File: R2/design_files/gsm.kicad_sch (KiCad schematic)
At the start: 23 parts, among them J4 Conn_Coaxial, J5 SIM_Card, M1 BG96, U3 PUMH10,115, U4 NXB0108PW, U5 AP22800HB-7, U6 DF6A6.8FUT

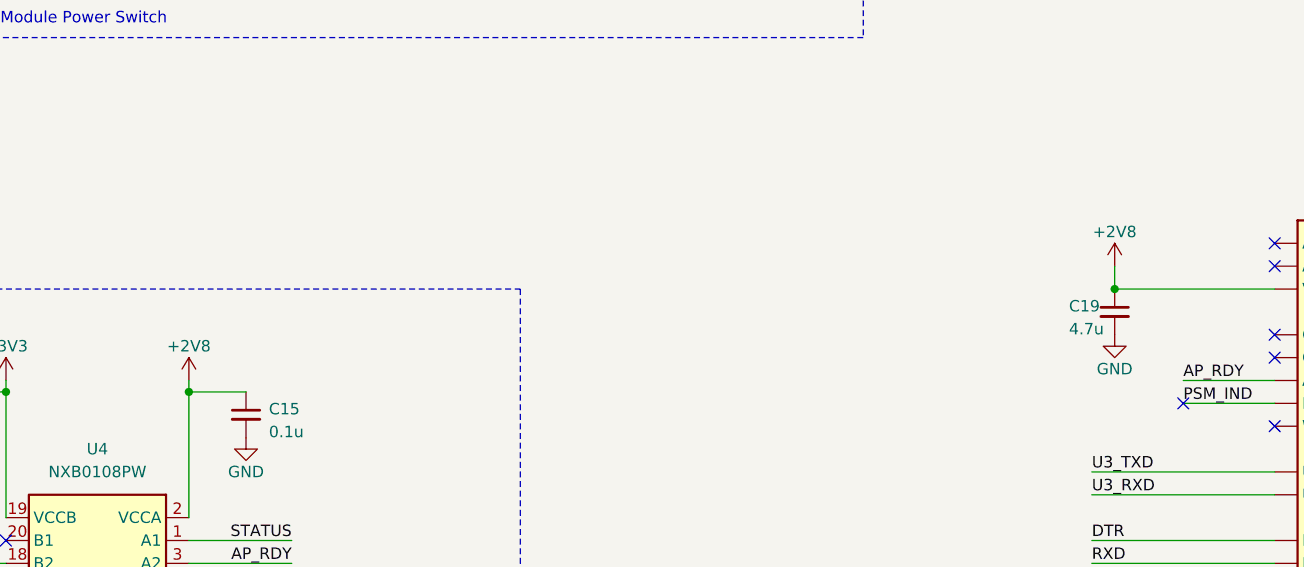
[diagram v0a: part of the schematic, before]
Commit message: Added test points
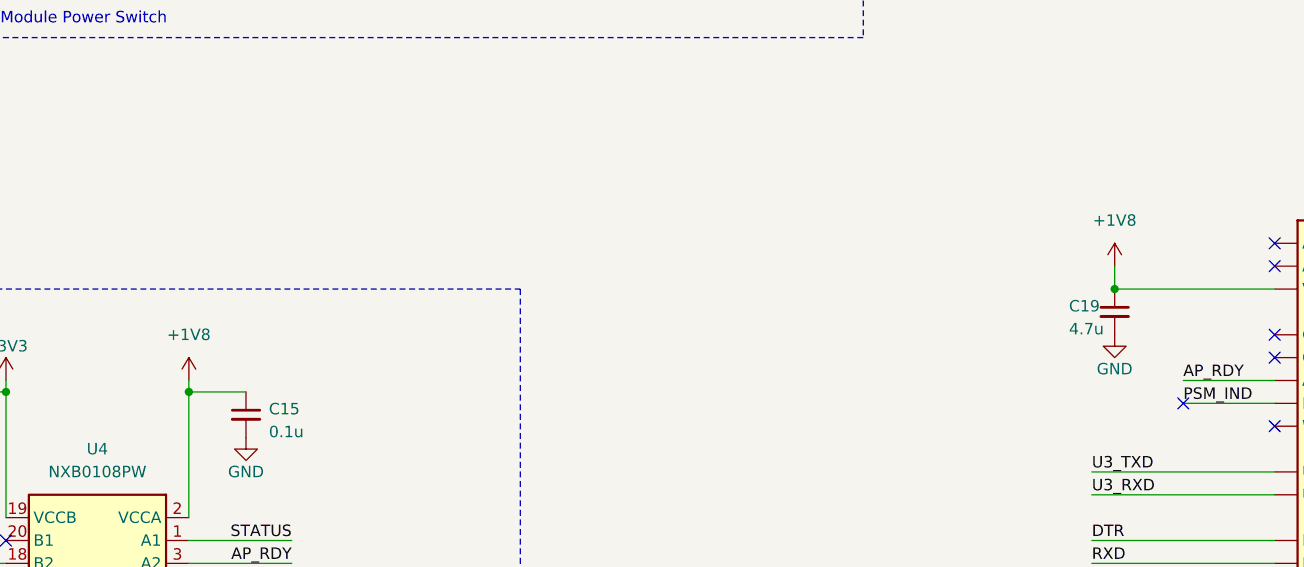
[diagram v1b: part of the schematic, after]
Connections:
- net +2V8 renamed +1V8
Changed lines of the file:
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@@
 			)
 		)
-		(property "Value" "+2V8"
-			(at 208.28 102.87 0)
+		(property "Value" "+1V8"
+			(at 208.28 101.6 0)
 			(effects
 				(font
@@
 			)
 		)
-		(property "Value" "+2V8"
-			(at 105.41 115.57 0)
-			(effects
-				(font
+		(property "Value" "+1V8"
+			(at 105.41 114.3 0)
+			(effects
+				(font
